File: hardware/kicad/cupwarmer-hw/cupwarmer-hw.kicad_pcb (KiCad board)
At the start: 4 copper layers, 56 x 56 mm, 48 parts, among them J1 I2C Service, J2 THERM_MON, J3 STATUS_MON, Q1 AO3400 SOT-23, U1 STWLC38JRM

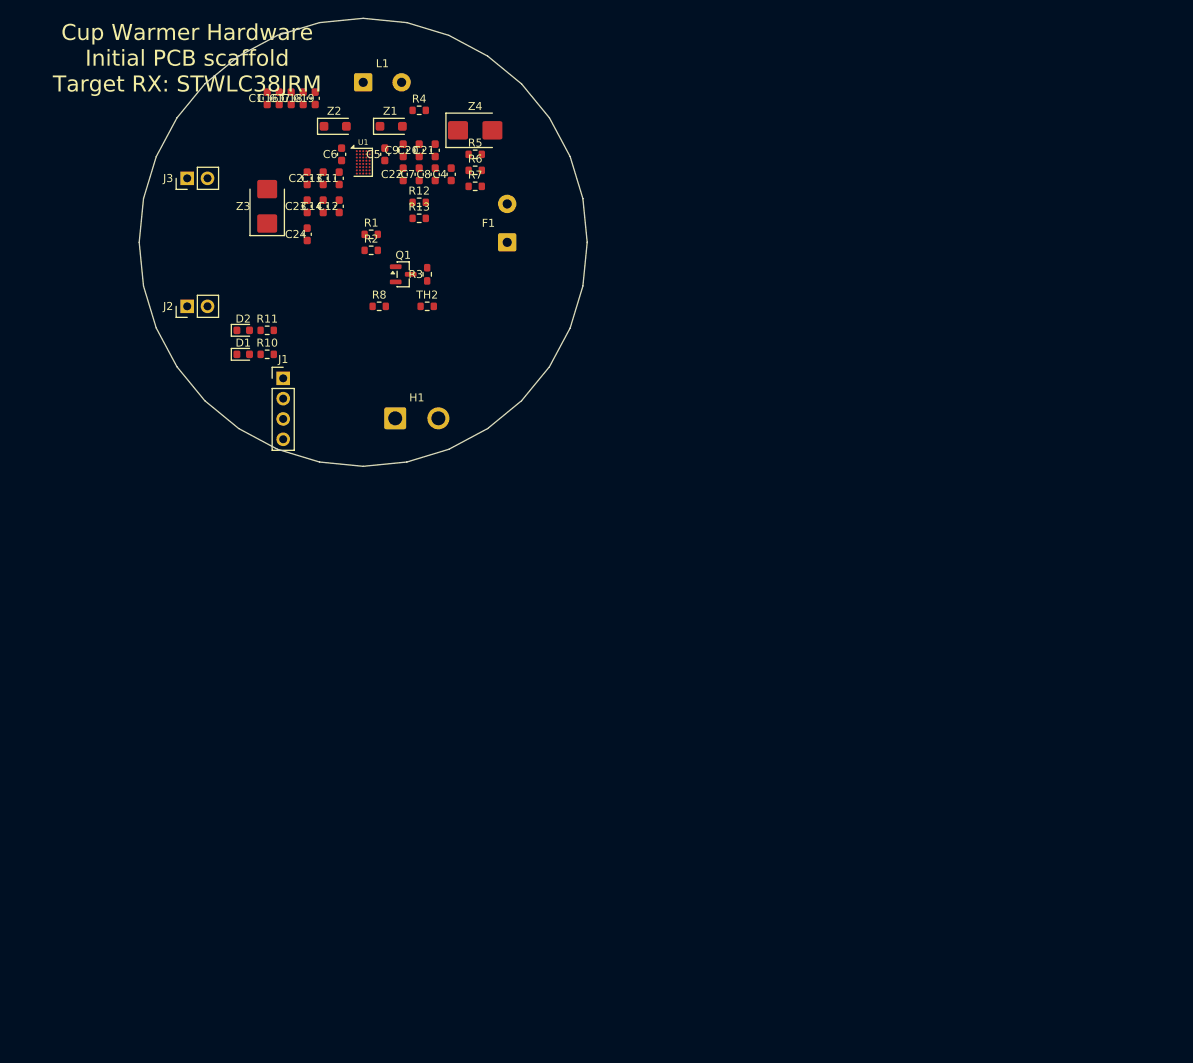
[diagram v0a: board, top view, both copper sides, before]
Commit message: Switch L1 footprint to Würth 760308102207 (P5.0mm)
Custom SolderWire footprint with 5.0mm pitch and φ1.2mm holes
matching the WE-WPCC 760308102207 lead pattern. Includes a
40×40mm rounded-square outline on Dwgs.User as a placement guide
for the coil module body. Schematic L1 properties (Value, MPN,
Manufacturer, LCSC, Footprint) updated to match the BOM.

ERC clean; PCB parity unchanged; no new DRC violations on L1.
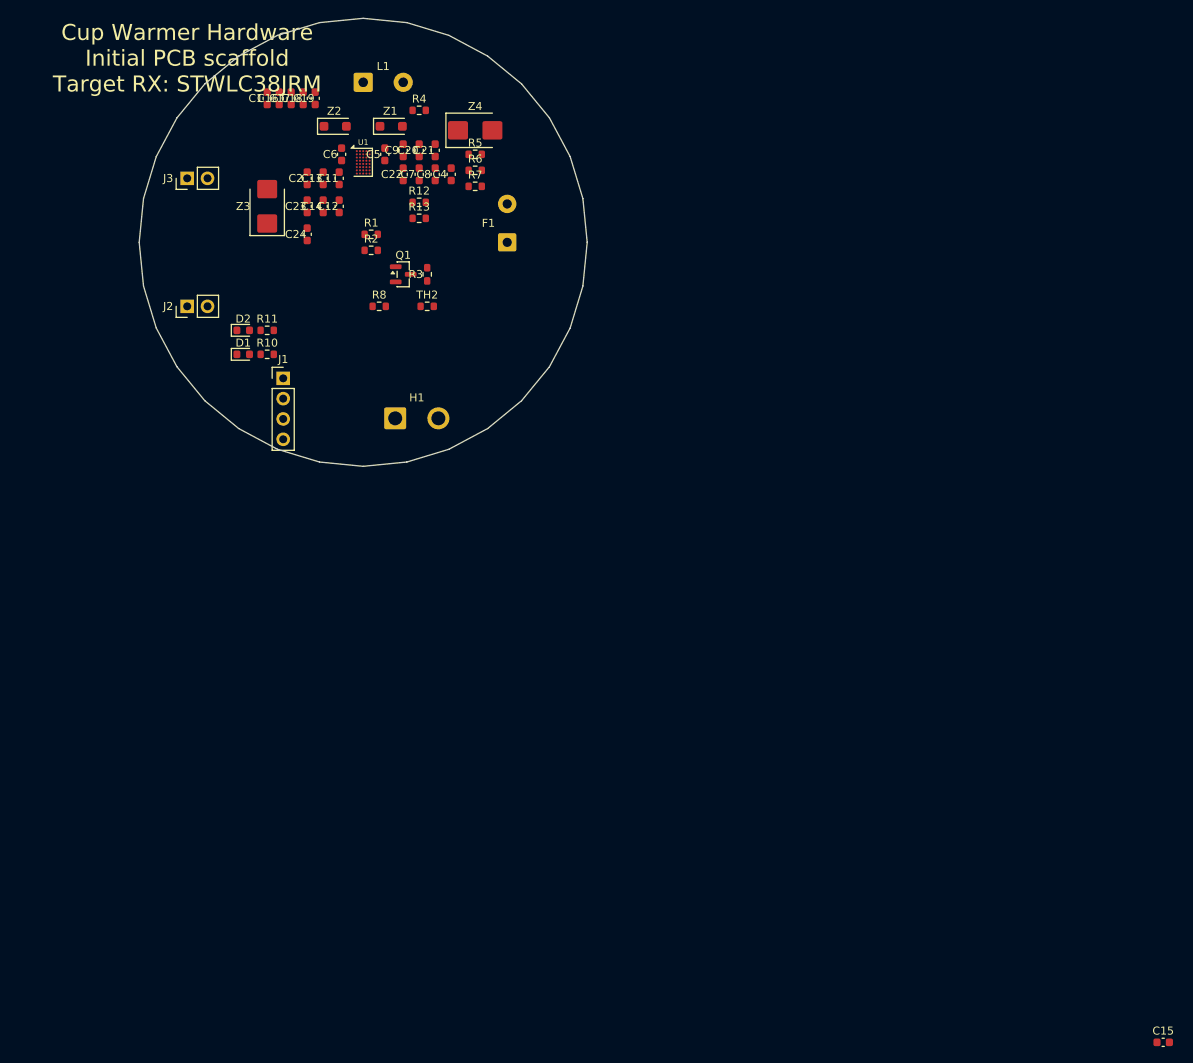
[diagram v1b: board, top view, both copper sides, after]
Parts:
- added C15: 3.3nF/50V, Capacitor_SMD:C_0603_1608Metric, F.Cu at (200.0, 200.0)
- L1: value YX-A11-R351125-G0265 8uH -> 8uH; footprint Connector_Wire:SolderWire-0.5sqmm_1x02_P4.8mm_D0.9mm_OD2.3mm -> cupwarmer:SolderWire-Wuerth760308_1x02_P5.0mm_D1.2mm
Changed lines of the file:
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@@
-		)
-	)
-	(footprint "Connector_Wire:SolderWire-0.5sqmm_1x02_P4.8mm_D0.9mm_OD2.3mm"
-		(layer "F.Cu")
-		(at 100 80 0)
-		(descr "Soldered wire connection, for 2 times 0.5 mm² wires, reinforced insulation, conductor diameter 0.9mm, outer diameter 2.3mm, size source Multi-Contact FLEXI-xV 0.50 (https://www.staubli.com/content/dam/ecs/catalogs-brochures/TM/CAB-Main-11014119-en.pdf#page=11), bend radius 3 times outer diameter")
-		(tags "connector wire 0.5sqmm")
-		(property "Reference" "L1"
-			(at 2.4 -2.35 0)
-			(layer "F.SilkS")
-			(effects
-				(font
-					(size 1 1)
-					(thickness 0.15)
-				)
-			)
-		)
-		(property "Value" "YX-A11-R351125-G0265 8uH"
-			(at 2.4 2.35 0)
-			(layer "F.Fab")
-			(effects
-				(font
-					(size 1 1)
-					(thickness 0.15)
-				)
-			)
-		)
-		(property "Datasheet" ""
-			(at 0 0 90)
-			(layer "F.Fab")
-			(hide yes)
-			(effects
-				(font
-					(size 1.27 1.27)
-				)
-			)
-		)
-		(property "Description" ""
-			(at 0 0 90)
-			(layer "F.Fab")
-			(hide yes)
-			(effects
-				(font
-					(size 1.27 1.27)
-				)
-			)
-		)
-		(property "KiLib_Generator" "connector/wire"
-			(at 0 0 0)
-			(layer "F.SilkS")
-			(hide yes)
-			(effects
-				(font
-					(size 1 1)
-					(thickness 0.15)
-				)
-			)
-		)
-		(attr exclude_from_pos_files exclude_from_bom)
-		(duplicate_pad_numbers_are_jumpers no)
-		(fp_rect
-			(start 2.9 -1.65)
-			(end 6.7 1.65)
-			(stroke
-				(width 0.05)
-				(type solid)
-			)
-			(fill no)
-			(layer "F.CrtYd")
-		)
-		(fp_rect
-			(start -1.9 -1.65)
-			(end 1.9 1.65)
-			(stroke
-				(width 0.05)
-				(type solid)
-			)
-			(fill no)
-			(layer "F.CrtYd")
-		)
-		(fp_circle
-			(center 4.8 0)
-			(end 5.95 0)
-			(stroke
-				(width 0.1)
-				(type solid)
-			)
-			(fill no)
-			(layer "F.Fab")
-		)
-		(fp_circle
-			(center 0 0)
-			(end 1.15 0)
-			(stroke
-				(width 0.1)
-				(type solid)
-			)
-			(fill no)
-			(layer "F.Fab")
-		)
-		(fp_text user "${REFERENCE}"
-			(at 2.4 0 90)
-			(layer "F.Fab")
-			(effects
-				(font
-					(size 0.82 0.82)
-					(thickness 0.12)
-				)
-			)
-		)
-		(pad "1" thru_hole roundrect
-			(at 0 0)
-			(size 2.3 2.3)
-			(drill 1.15)
-			(layers "*.Cu" "*.Mask")
-			(remove_unused_layers no)
-			(roundrect_rratio 0.108696)
-		)
-		(pad "2" thru_hole circle
-			(at 4.8 0)
-			(size 2.3 2.3)
-			(drill 1.15)
-			(layers "*.Cu" "*.Mask")
-			(remove_unused_layers no)
-		)
-		(embedded_fonts no)
-		(model "${KICAD10_3DMODEL_DIR}/Connector_Wire.3dshapes/SolderWire-0.5sqmm_1x02_P4.8mm_D0.9mm_OD2.3mm.step"
-			(offset
-				(xyz 0 0 0)
-			)
-			(scale
-				(xyz 1 1 1)
-			)
-			(rotate
-				(xyz 0 0 0)
-			)
 		)
 	)
@@
 	)
 	(embedded_fonts no)
+	(footprint "Capacitor_SMD:C_0603_1608Metric"
+		(layer "F.Cu")
+		(at 200 200 0)
+		(descr "Capacitor SMD 0603 (1608 Metric), square (rectangular) end terminal, IPC-7351 nominal, (Body size source: IPC-SM-782 page 76, https://www.pcb-3d.com/wordpress/wp-content/uploads/ipc-sm-782a_amendment_1_and_2.pdf)")
+		(tags "capacitor")
+		(property "Reference" "C15"
+			(at 0 -1.43 0)
+			(layer "F.SilkS")
+			(effects
+				(font
+					(size 1 1)
+					(thickness 0.15)
+				)
+			)
+		)
+		(property "Value" "3.3nF/50V"
+			(at 0 1.43 0)
+			(layer "F.Fab")
+			(effects
+				(font
+					(size 1 1)
+					(thickness 0.15)
+				)
+			)
+		)
+		(property "KiLib_Generator" "SMD_2terminal_chip_molded"
+			(at 0 0 0)
+			(layer "F.SilkS")
+			(hide yes)
+			(effects
+				(font
+					(size 1 1)
+					(thickness 0.15)
+				)
+			)
+		)
+		(attr smd)
+		(duplicate_pad_numbers_are_jumpers no)
+		(fp_line
+			(start -0.14058 -0.51)
+			(end 0.14058 -0.51)
+			(stroke
+				(width 0.12)
+				(type solid)
+			)
+			(layer "F.SilkS")
+		)
+		(fp_line
+			(start -0.14058 0.51)
+			(end 0.14058 0.51)
+			(stroke
+				(width 0.12)
+				(type solid)
+			)
+			(layer "F.SilkS")
+		)
+		(fp_rect
+			(start -1.48 -0.73)
+			(end 1.48 0.73)
+			(stroke
+				(width 0.05)
+				(type solid)
+			)
+			(fill no)
+			(layer "F.CrtYd")
+		)
+		(fp_rect
+			(start -0.8 -0.4)
+			(end 0.8 0.4)
+			(stroke
+				(width 0.1)
+				(type solid)
+			)
+			(fill no)
+			(layer "F.Fab")
+		)
+		(fp_text user "${REFERENCE}"
+			(at 0 0 0)
+			(layer "F.Fab")
+			(effects
+				(font
+					(size 0.4 0.4)
+					(thickness 0.06)
+				)
+			)
+		)
+		(pad "1" smd roundrect
+			(at -0.775 0)
+			(size 0.9 0.95)
+			(layers "F.Cu" "F.Mask" "F.Paste")
+			(roundrect_rratio 0.25)
+		)
+		(pad "2" smd roundrect
+			(at 0.775 0)
+			(size 0.9 0.95)
+			(layers "F.Cu" "F.Mask" "F.Paste")
+			(roundrect_rratio 0.25)
+		)
+		(embedded_fonts no)
+		(model "${KICAD10_3DMODEL_DIR}/Capacitor_SMD.3dshapes/C_0603_1608Metric.step"
+			(offset
+				(xyz 0 0 0)
+			)
+			(scale
+				(xyz 1 1 1)
+			)
+			(rotate
+				(xyz 0 0 0)
+			)
+		)
+	)
+	(footprint "cupwarmer:SolderWire-Wuerth760308_1x02_P5.0mm_D1.2mm"
+		(layer "F.Cu")
+		(at 100 80 0)
+		(descr "Soldered wire pads for Würth 760308102207 RX coil leads, P5.0 mm, hole 1.2 mm")
+		(tags "connector wire coil wuerth 760308")
+		(property "Reference" "L1"
+			(at 2.5 -2.0 0)
+			(layer "F.SilkS")
+			(effects
+				(font
+					(size 1 1)
+					(thickness 0.15)
+				)
+			)
+		)
+		(property "Value" "8uH"
+			(at 2.5 2.0 0)
+			(layer "F.Fab")
+			(effects
+				(font
+					(size 1 1)
+					(thickness 0.15)
+				)
+			)
+		)
+		(property "KiLib_Generator" "connector/wire"
+			(at 0 0 0)
+			(layer "F.SilkS")
+			(hide yes)
+			(effects
+				(font
+					(size 1 1)
+					(thickness 0.15)
+				)
+			)
+		)
+		(attr exclude_from_pos_files exclude_from_bom)
+		(duplicate_pad_numbers_are_jumpers no)
+		(fp_rect
+			(start -1.5 -1.5)
+			(end 1.5 1.5)
+			(stroke
+				(width 0.05)
+				(type solid)
+			)
+			(fill no)
+			(layer "F.CrtYd")
+		)
+		(fp_rect
+			(start 3.5 -1.5)
+			(end 6.5 1.5)
+			(stroke
+				(width 0.05)
+				(type solid)
+			)
+			(fill no)
+			(layer "F.CrtYd")
+		)
+		(fp_circle
+			(center 0 0)
+			(end 1.2 0)
+			(stroke
+				(width 0.1)
+				(type solid)
+			)
+			(fill no)
+			(layer "F.Fab")
+		)
+		(fp_circle
+			(center 5.0 0)
+			(end 6.2 0)
+			(stroke
+				(width 0.1)
+				(type solid)
+			)
+			(fill no)
+			(layer "F.Fab")
+		)
+		(fp_text user "${REFERENCE}"
+			(at 2.5 0 90)
+			(layer "F.Fab")
+			(effects
+				(font
+					(size 0.94 0.94)
+					(thickness 0.14)
+				)
+			)
+		)
+		(fp_line (start -12.5 -20) (end 17.5 -20) (stroke (width 0.1) (type solid)) (layer "Dwgs.User"))
+		(fp_line (start -17.5 -15) (end -17.5 15) (stroke (width 0.1) (type solid)) (layer "Dwgs.User"))
+		(fp_line (start -12.5 20) (end 17.5 20) (stroke (width 0.1) (type solid)) (layer "Dwgs.User"))
+		(fp_line (start 22.5 -15) (end 22.5 15) (stroke (width 0.1) (type solid)) (layer "Dwgs.User"))
+		(fp_arc (start -12.5 -20) (mid -16.036 -16.464) (end -17.5 -15) (stroke (width 0.1) (type solid)) (layer "Dwgs.User"))
+		(fp_arc (start -17.5 15) (mid -16.036 16.464) (end -12.5 20) (stroke (width 0.1) (type solid)) (layer "Dwgs.User"))
+		(fp_arc (start 17.5 20) (mid 21.036 16.464) (end 22.5 15) (stroke (width 0.1) (type solid)) (layer "Dwgs.User"))
+		(fp_arc (start 22.5 -15) (mid 21.036 -16.464) (end 17.5 -20) (stroke (width 0.1) (type solid)) (layer "Dwgs.User"))
+		(pad "1" thru_hole roundrect
+			(at 0 0)
+			(size 2.4 2.4)
+			(drill 1.2)
+			(layers "*.Cu" "*.Mask")
+			(remove_unused_layers no)
+			(roundrect_rratio 0.104167)
+		)
+		(pad "2" thru_hole circle
+			(at 5.0 0)
+			(size 2.4 2.4)
+			(drill 1.2)
+			(layers "*.Cu" "*.Mask")
+			(remove_unused_layers no)
+		)
+		(embedded_fonts no)
+	)
 )

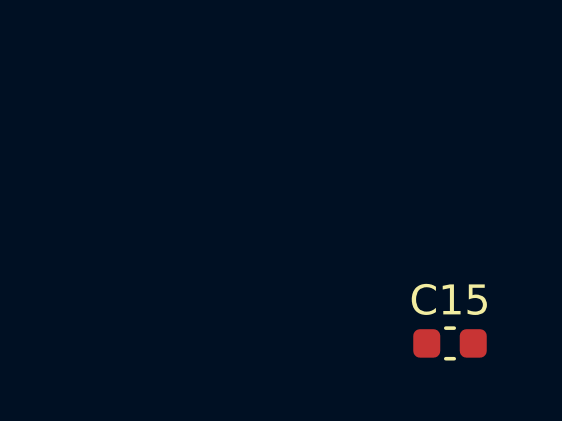
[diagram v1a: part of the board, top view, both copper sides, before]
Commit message: Actually drop C15 (Cd) symbol + footprint
Earlier 522ecc1 commit removed the BOM row but the kicad-tool
delete on the schematic silently no-op'd, leaving C15 in
rx-power.kicad_sch and the PCB. This commit deletes the symbol,
its two dangling wire stubs, and the footprint. ERC clean.
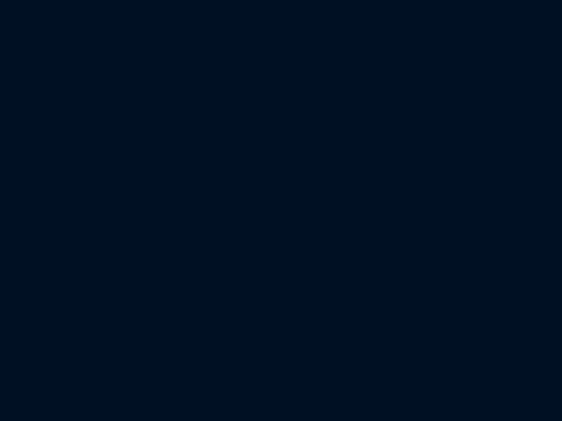
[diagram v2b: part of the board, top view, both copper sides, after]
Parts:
- removed C15: 3.3nF/50V, Capacitor_SMD:C_0603_1608Metric
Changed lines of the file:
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@@
 	)
 	(embedded_fonts no)
-	(footprint "Capacitor_SMD:C_0603_1608Metric"
-		(layer "F.Cu")
-		(at 200 200 0)
-		(descr "Capacitor SMD 0603 (1608 Metric), square (rectangular) end terminal, IPC-7351 nominal, (Body size source: IPC-SM-782 page 76, https://www.pcb-3d.com/wordpress/wp-content/uploads/ipc-sm-782a_amendment_1_and_2.pdf)")
-		(tags "capacitor")
-		(property "Reference" "C15"
-			(at 0 -1.43 0)
-			(layer "F.SilkS")
-			(effects
-				(font
-					(size 1 1)
-					(thickness 0.15)
-				)
-			)
-		)
-		(property "Value" "3.3nF/50V"
-			(at 0 1.43 0)
-			(layer "F.Fab")
-			(effects
-				(font
-					(size 1 1)
-					(thickness 0.15)
-				)
-			)
-		)
-		(property "KiLib_Generator" "SMD_2terminal_chip_molded"
-			(at 0 0 0)
-			(layer "F.SilkS")
-			(hide yes)
-			(effects
-				(font
-					(size 1 1)
-					(thickness 0.15)
-				)
-			)
-		)
-		(attr smd)
-		(duplicate_pad_numbers_are_jumpers no)
-		(fp_line
-			(start -0.14058 -0.51)
-			(end 0.14058 -0.51)
-			(stroke
-				(width 0.12)
-				(type solid)
-			)
-			(layer "F.SilkS")
-		)
-		(fp_line
-			(start -0.14058 0.51)
-			(end 0.14058 0.51)
-			(stroke
-				(width 0.12)
-				(type solid)
-			)
-			(layer "F.SilkS")
-		)
-		(fp_rect
-			(start -1.48 -0.73)
-			(end 1.48 0.73)
-			(stroke
-				(width 0.05)
-				(type solid)
-			)
-			(fill no)
-			(layer "F.CrtYd")
-		)
-		(fp_rect
-			(start -0.8 -0.4)
-			(end 0.8 0.4)
-			(stroke
-				(width 0.1)
-				(type solid)
-			)
-			(fill no)
-			(layer "F.Fab")
-		)
-		(fp_text user "${REFERENCE}"
-			(at 0 0 0)
-			(layer "F.Fab")
-			(effects
-				(font
-					(size 0.4 0.4)
-					(thickness 0.06)
-				)
-			)
-		)
-		(pad "1" smd roundrect
-			(at -0.775 0)
-			(size 0.9 0.95)
-			(layers "F.Cu" "F.Mask" "F.Paste")
-			(roundrect_rratio 0.25)
-		)
-		(pad "2" smd roundrect
-			(at 0.775 0)
-			(size 0.9 0.95)
-			(layers "F.Cu" "F.Mask" "F.Paste")
-			(roundrect_rratio 0.25)
-		)
-		(embedded_fonts no)
-		(model "${KICAD10_3DMODEL_DIR}/Capacitor_SMD.3dshapes/C_0603_1608Metric.step"
-			(offset
-				(xyz 0 0 0)
-			)
-			(scale
-				(xyz 1 1 1)
-			)
-			(rotate
-				(xyz 0 0 0)
-			)
-		)
-	)
 	(footprint "cupwarmer:SolderWire-Wuerth760308_1x02_P5.0mm_D1.2mm"
 		(layer "F.Cu")
